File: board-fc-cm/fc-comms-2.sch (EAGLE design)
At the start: 228 parts, among them IC1 TPS79930QDDCRQ1, IC11 MPU-9250, IC12 TXB0108PW, IC13 TPS3813K33-EP_DBV_6, IC14 TMP100-EP_DBV_6, IC15 LHA1+, IC16 PCT2075TP, IC17 MMZ09332BT1, IC18 PCT2075TP, IC2 TPS79930QDDCRQ1, IC3 MSP430FR2311PW, IC4 MCP1700TT, IC5 TXB0108PW, IC6 TXB0108PW, IC7 CC1125RHBT, IC77 74LVC1G08, IC8 CC1125RHBT, IC9 TM4C123[7,G]XXPM, J3 SWD_SHROUD, Q3 32.768kHz, Q4 BSS123, Q5 BSS84, X1 SHIELD-26X26, X12 BU-SMA-V, X18 BU-SMA-V, X2 SHIELD-26X26, X3 LFTCXO070, X4 LFTCXO070, X5 SHIELD-26X26, X6 SHIELD-26X26, Y1 8MHz

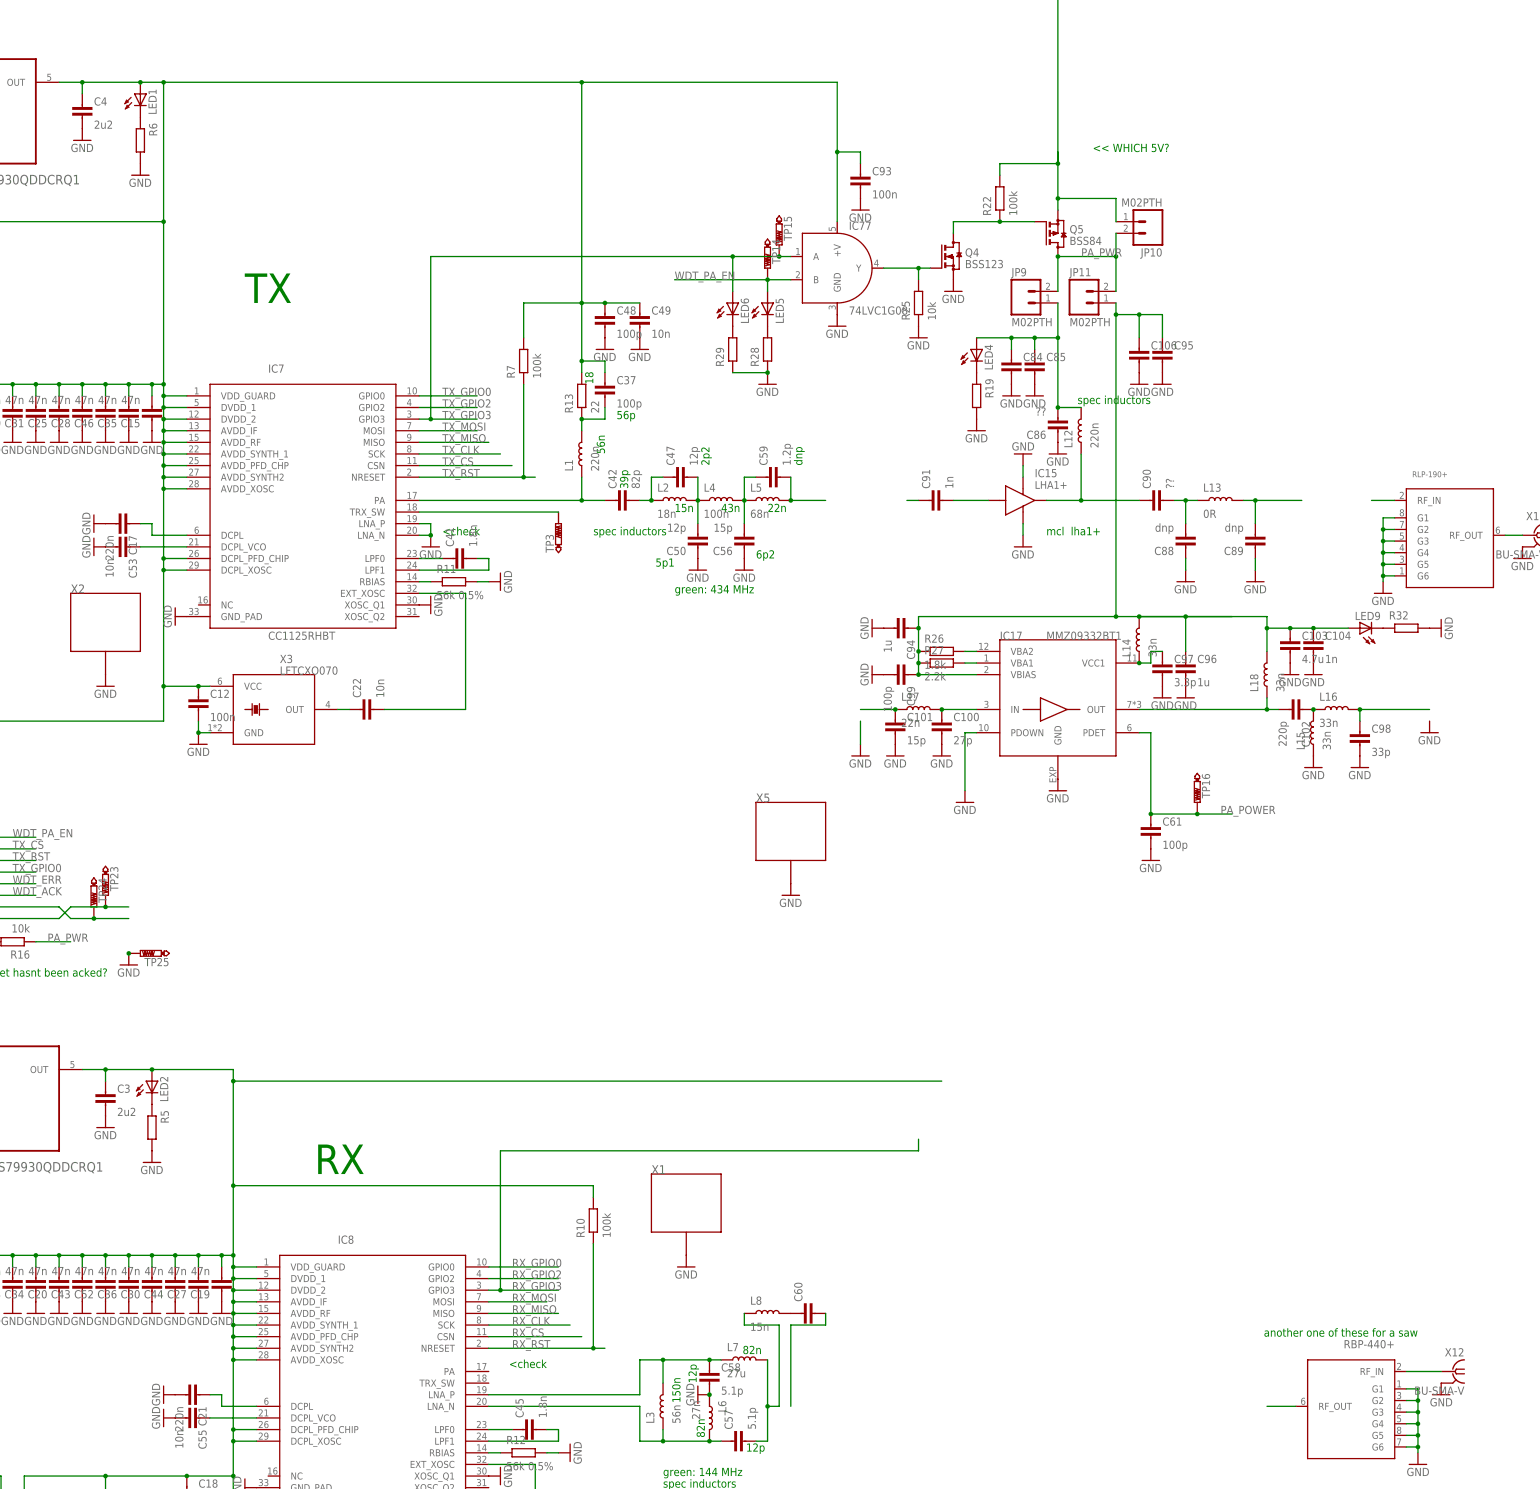
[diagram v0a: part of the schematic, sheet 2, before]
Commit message: adding fram, some routing
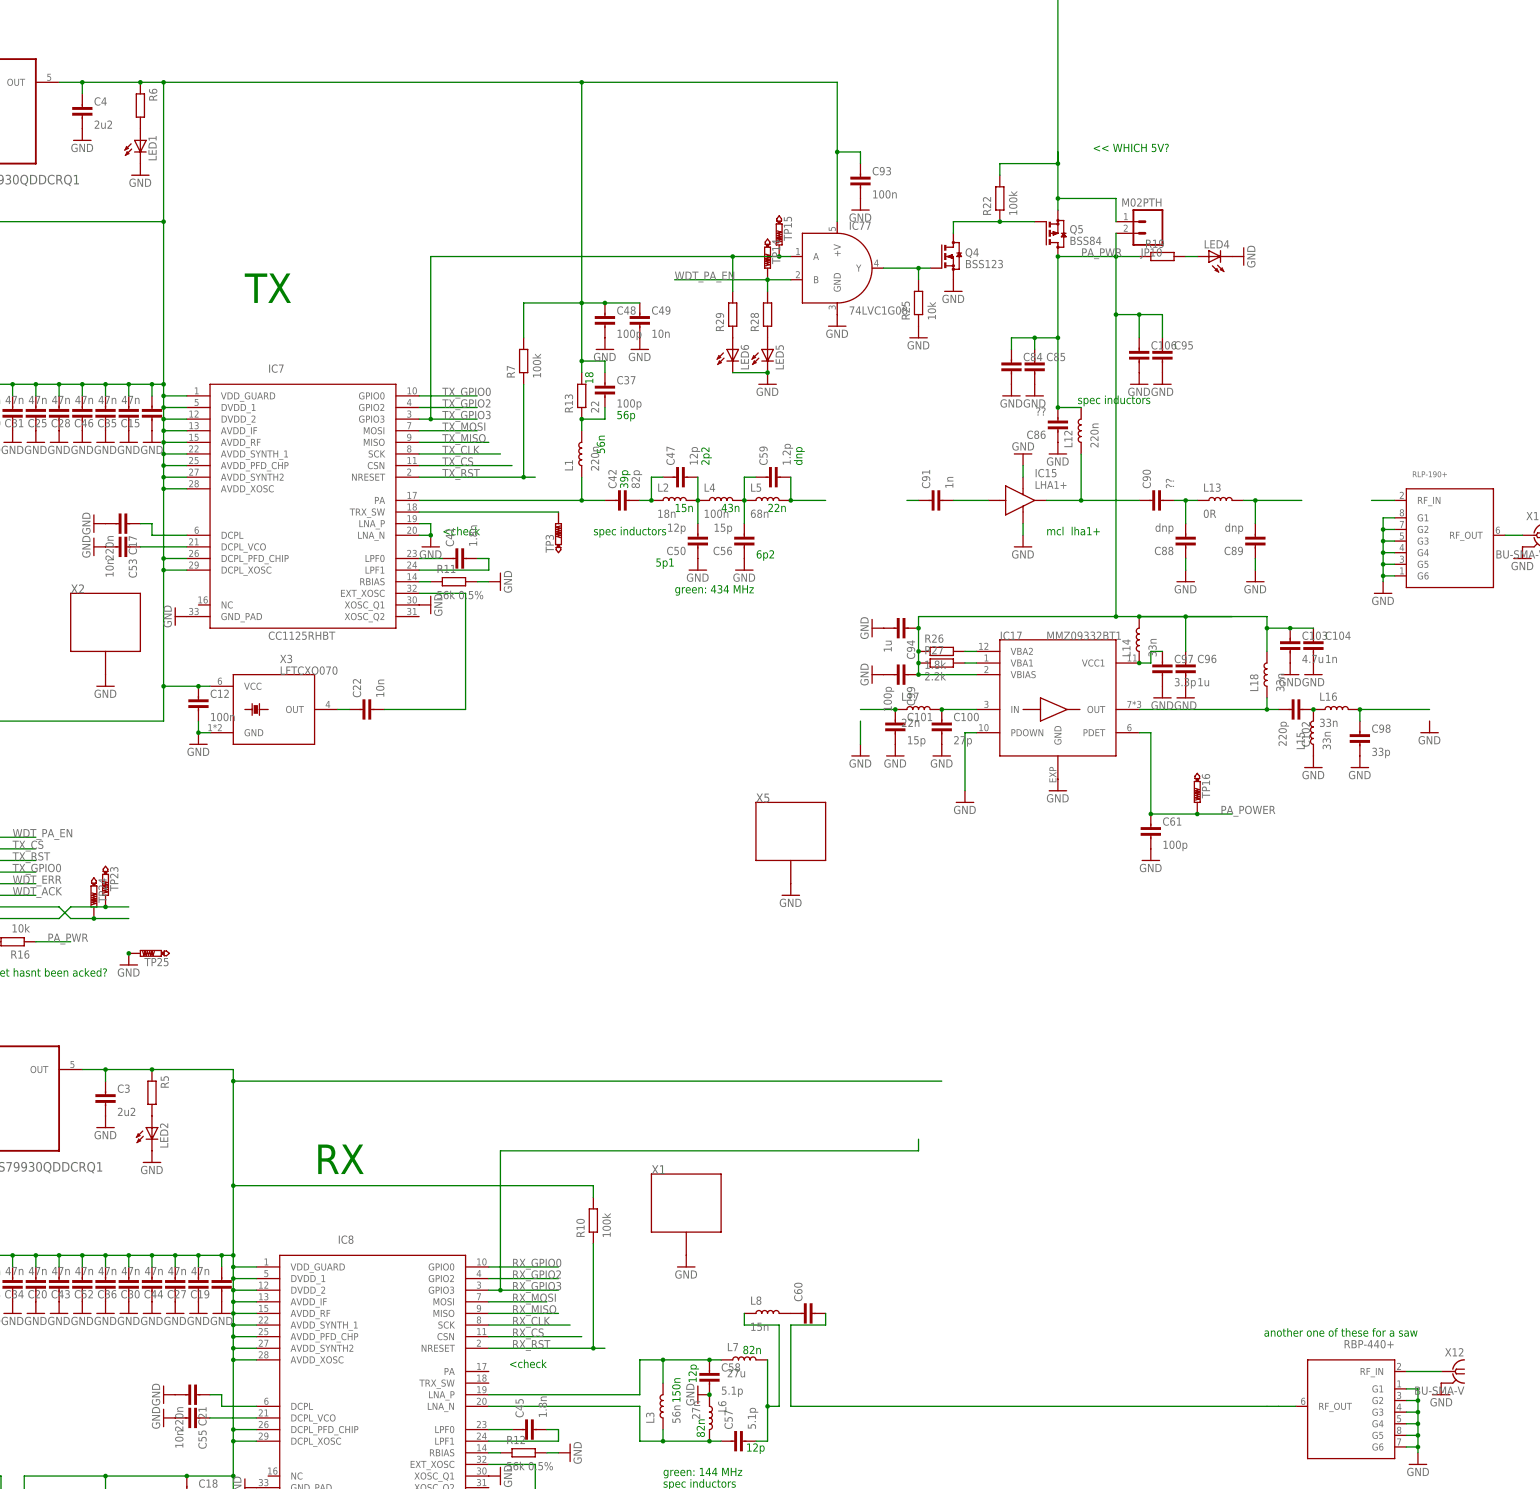
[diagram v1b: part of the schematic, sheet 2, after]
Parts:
- removed JP11, JP9: M02PTH, SparkFun-Connectors:M02PTH
- removed LED9: (no value), dtb:LEDCHIP-LED0603
- removed R32: (no value), passives-7351:RESISTOR0603-N
- added C8: 0.1u, passives-7351:CAPACITOR0603-N
- added IC10: FM25V10, cube-parts:FM25V10
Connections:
- removed net N$101: C60.2
- removed net N$24: C103.1, C104.1, C106.1, C94.1, C95.1, C96.1, C99.1, IC17.VBIAS, JP11.1, L14.P$2, L18.P$2, LED9.A, R26.P$1, R27.P$1
- removed net N$66: LED1.C, R6.P$1
- removed net N$67: LED2.C, R5.P$1
- removed net N$83: C84.1, C85.1, C86.2, JP9.1, L12.P$2, LED4.A
- removed net N$84: LED4.C, R19.P$1
- removed net N$85: LED9.C, R32.P$1
- new net FRAM_CS: IC10.!CS, IC9.PD6
- new net N$10: LED5.A, R28.P$1
- new net N$25: LED6.A, R29.P$1
- new net N$46: LED2.A, R5.P$2
- net 3V3/FMCU: now also C8.1, IC10.!HOLD, IC10.!WP, IC10.VCC
- net GND: now also C8.2, IC10.GND, LED1.C, LED2.C, LED4.C, LED5.C, LED6.C; no longer R19.P$2, R28.P$1, R29.P$1, R32.P$2, R5.P$2, R6.P$2
- net N$38: now also LED4.A, R19.P$2; no longer LED5.C, R28.P$2
- net N$40: now also R6.P$1; no longer LED1.A
- net N$41: now also LED1.A, R6.P$2; no longer LED6.C, R29.P$2
- net N$53: now also R5.P$1; no longer LED2.A
- net N$56: now also C60.2
- net PA_PWR: now also C103.1, C104.1, C106.1, C84.1, C85.1, C86.2, C94.1, C95.1, C96.1, C99.1, IC17.VBIAS, L12.P$2, L14.P$2, L18.P$2, R19.P$1, R26.P$1, R27.P$1; no longer JP11.2, JP9.2
- net TC/TXRX/CLK: now also IC10.SCK
- net TC/TXRX/MISO: now also IC10.SO
- net TC/TXRX/MOSI: now also IC10.SI
- net TX_GPIO3: now also R29.P$2; no longer LED6.A
- net WDT_PA_EN: now also R28.P$2; no longer LED5.A
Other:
- moved on the sheet: LED1, LED2, LED4, LED5, LED6, R19, R28, R29, R5, R6

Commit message: most routing done, still some queries remain
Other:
- note added: "WHERE DO WE CONNECT THE CAM TO?"
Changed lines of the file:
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@@
 <text x="431.8" y="109.22" size="1.778" layer="91">&lt;&lt; SURE 3V3 SYS ?</text>
 <text x="403.86" y="182.88" size="1.778" layer="91">NOTE! 3V3/SYS changed to 3V3/FMCU</text>
+<text x="287.02" y="106.68" size="1.778" layer="91">WHERE DO WE CONNECT THE CAM TO?</text>
+<text x="289.56" y="101.6" size="1.778" layer="91">WHERE DO WE CONNECT THE CAM TO?</text>
+<text x="304.8" y="71.12" size="1.778" layer="91" rot="R90">WHERE DO WE CONNECT THE CAM TO?</text>
 </plain>
 <instances>

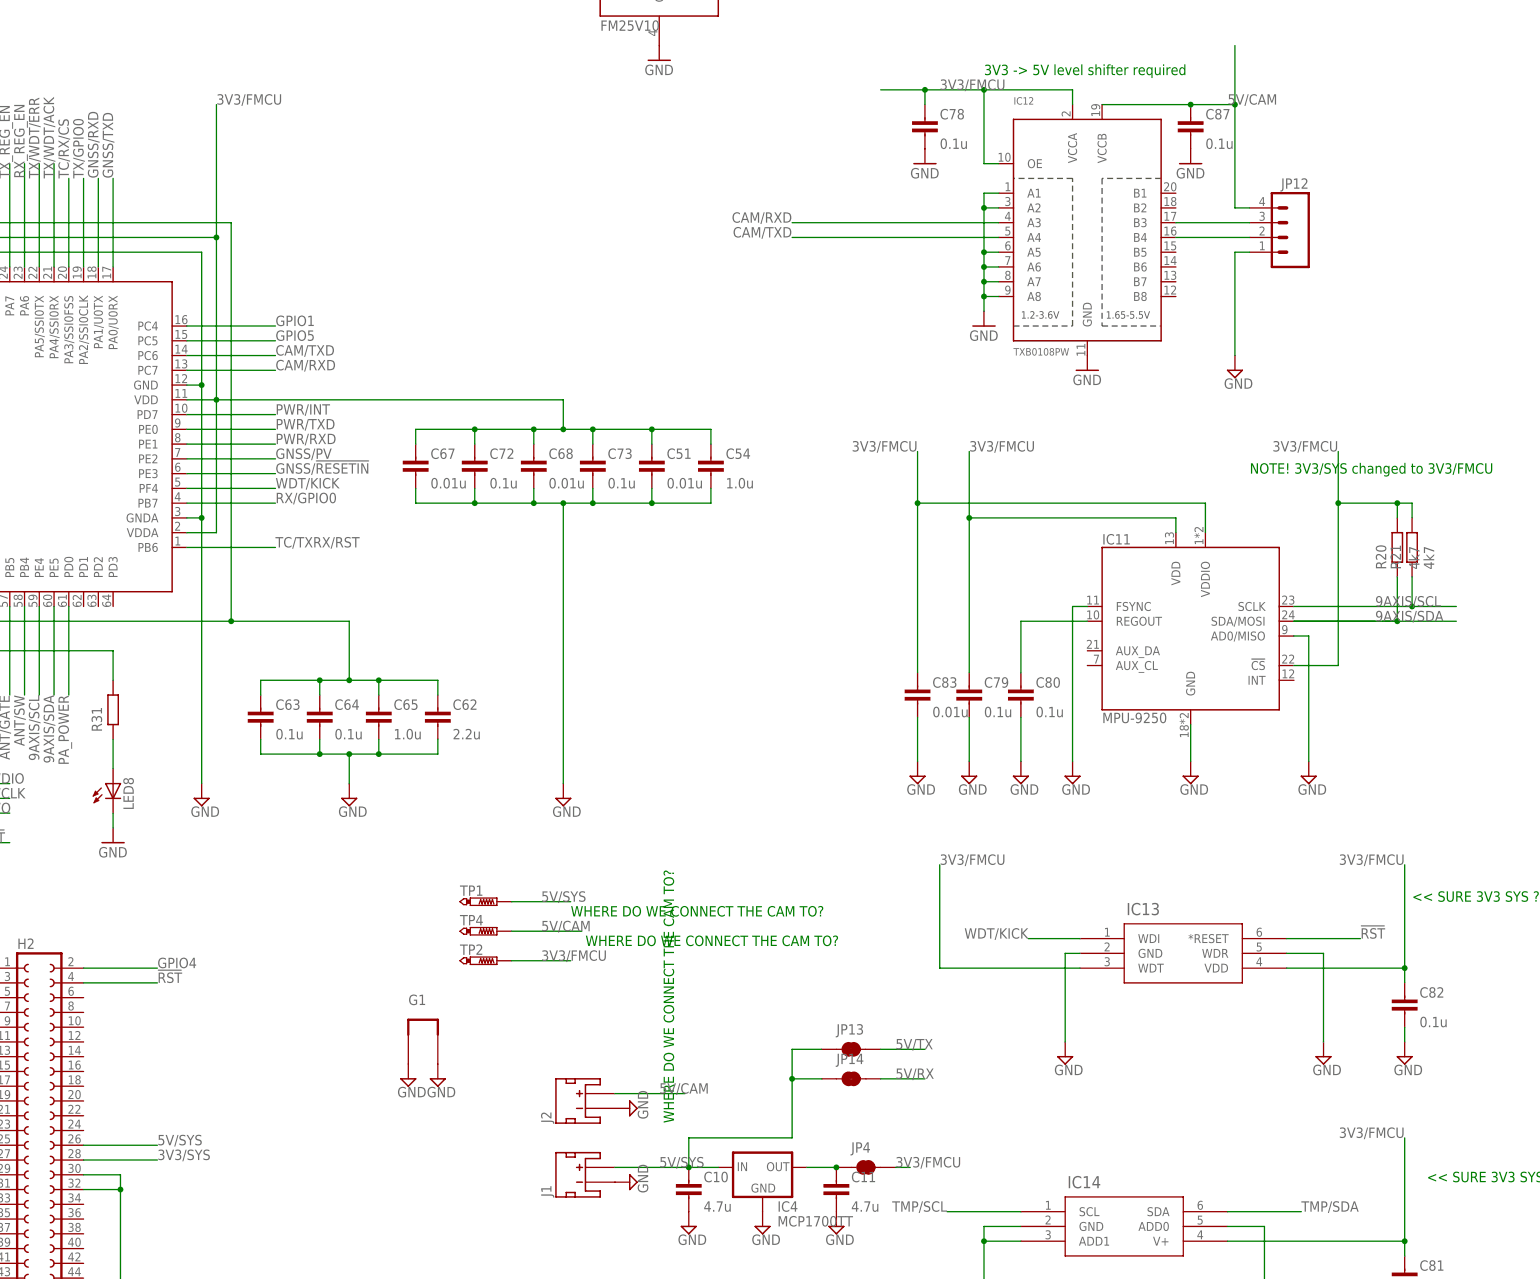
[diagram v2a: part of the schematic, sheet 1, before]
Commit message: added camera header, RF connectors, some cleanup
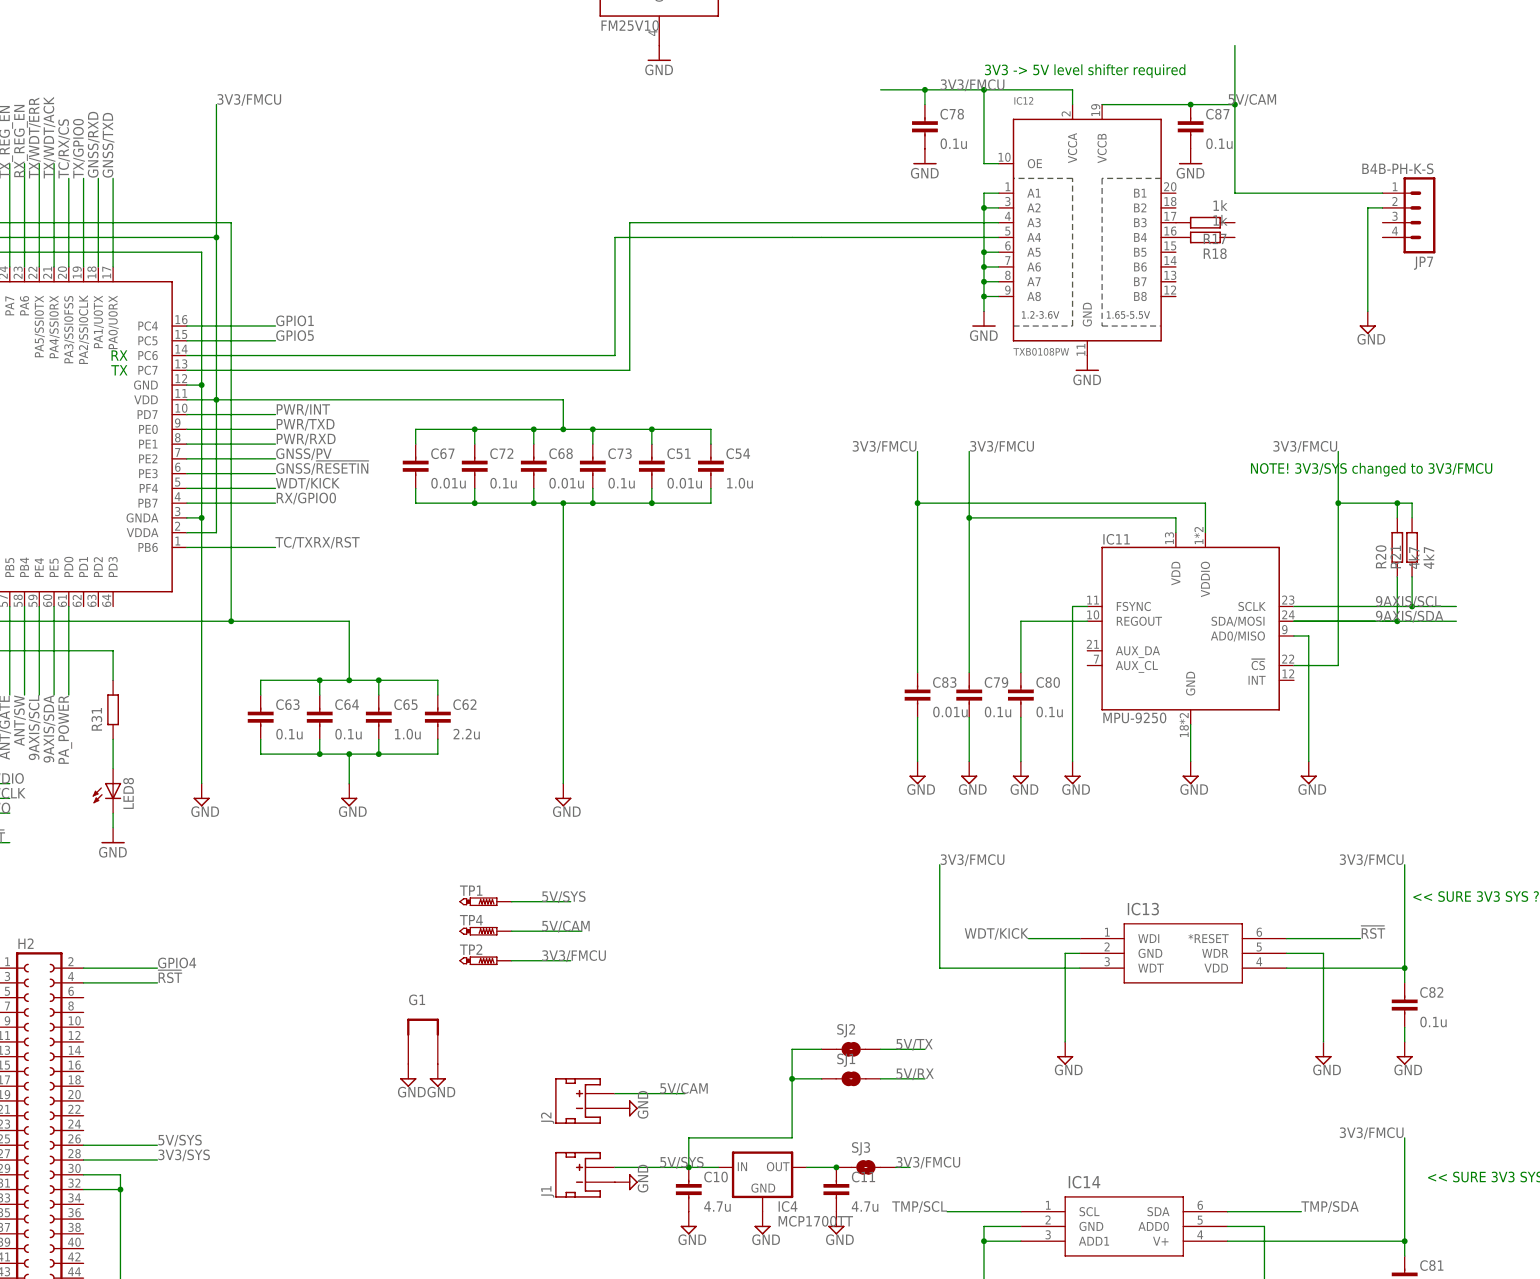
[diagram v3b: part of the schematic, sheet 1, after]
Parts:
- removed JP12: (no value), SparkFun-Connectors:M04PTH
- removed JP13, JP14, JP4: JUMPER-SMT_2_NC_TRACE_SILK, SparkFun-Jumpers:JUMPER-SMT_2_NC_TRACE_SILK
- removed X12, X18: BU-SMA-V, con-coax:BU-SMA-V
- added JP7: B4B-PH-K-S, cube-parts:B4B-PH-K-S
- added JP8, JP9: MCX, cube-parts:MCX
- added R17, R18: 1k, passives-7351:RESISTOR0603-N
- added SJ1, SJ2, SJ3: JUMPER-PAD-2-NOYES_SILK, SparkFun-Passives:JUMPER-PAD-2-NOYES_SILK
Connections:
- removed net N$61: IC12.B3, JP12.3
- removed net N$73: IC12.B4, JP12.2
- new net N$50: IC12.B3, R17.P$2
- new net N$52: IC12.B4, R18.P$2
- net 3V3/FMCU: now also SJ3.2; no longer JP4.2
- net 5V/CAM: now also JP7.1; no longer JP12.4
- net 5V/RX: now also SJ1.2; no longer JP14.2
- net 5V/SYS: now also SJ1.1, SJ2.1; no longer JP13.1, JP14.1
- net 5V/TX: now also SJ2.2; no longer JP13.2
- net GND: now also JP7.2, JP8.2, JP9.2; no longer JP12.1, X12.2, X18.2
- net N$29: now also JP8.1; no longer X18.1
- net N$55: now also JP9.1; no longer X12.1
- net N$64: now also SJ3.1; no longer JP4.1
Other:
- note removed: "WHERE DO WE CONNECT THE CAM TO?"
